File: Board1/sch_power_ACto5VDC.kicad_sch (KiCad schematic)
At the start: 9 parts, among them J1 240VAC

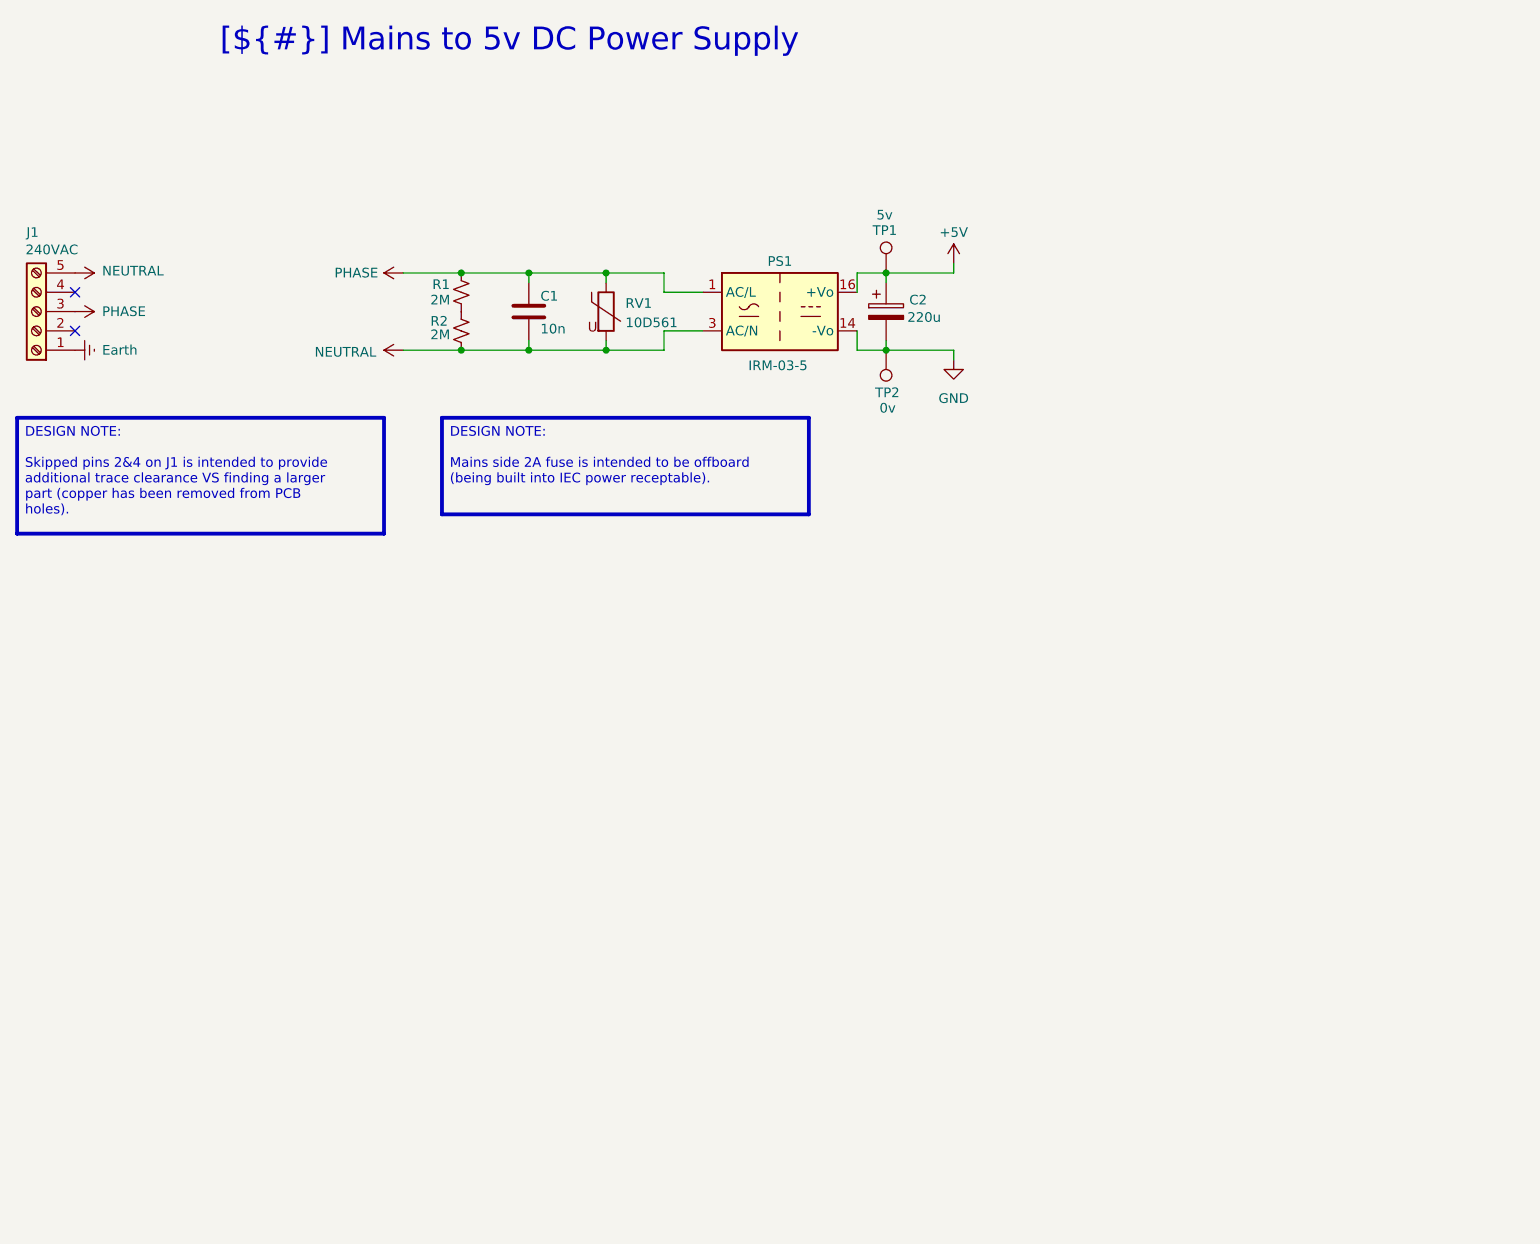
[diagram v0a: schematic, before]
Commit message: Resolve library and ERC issues
No changes to design.
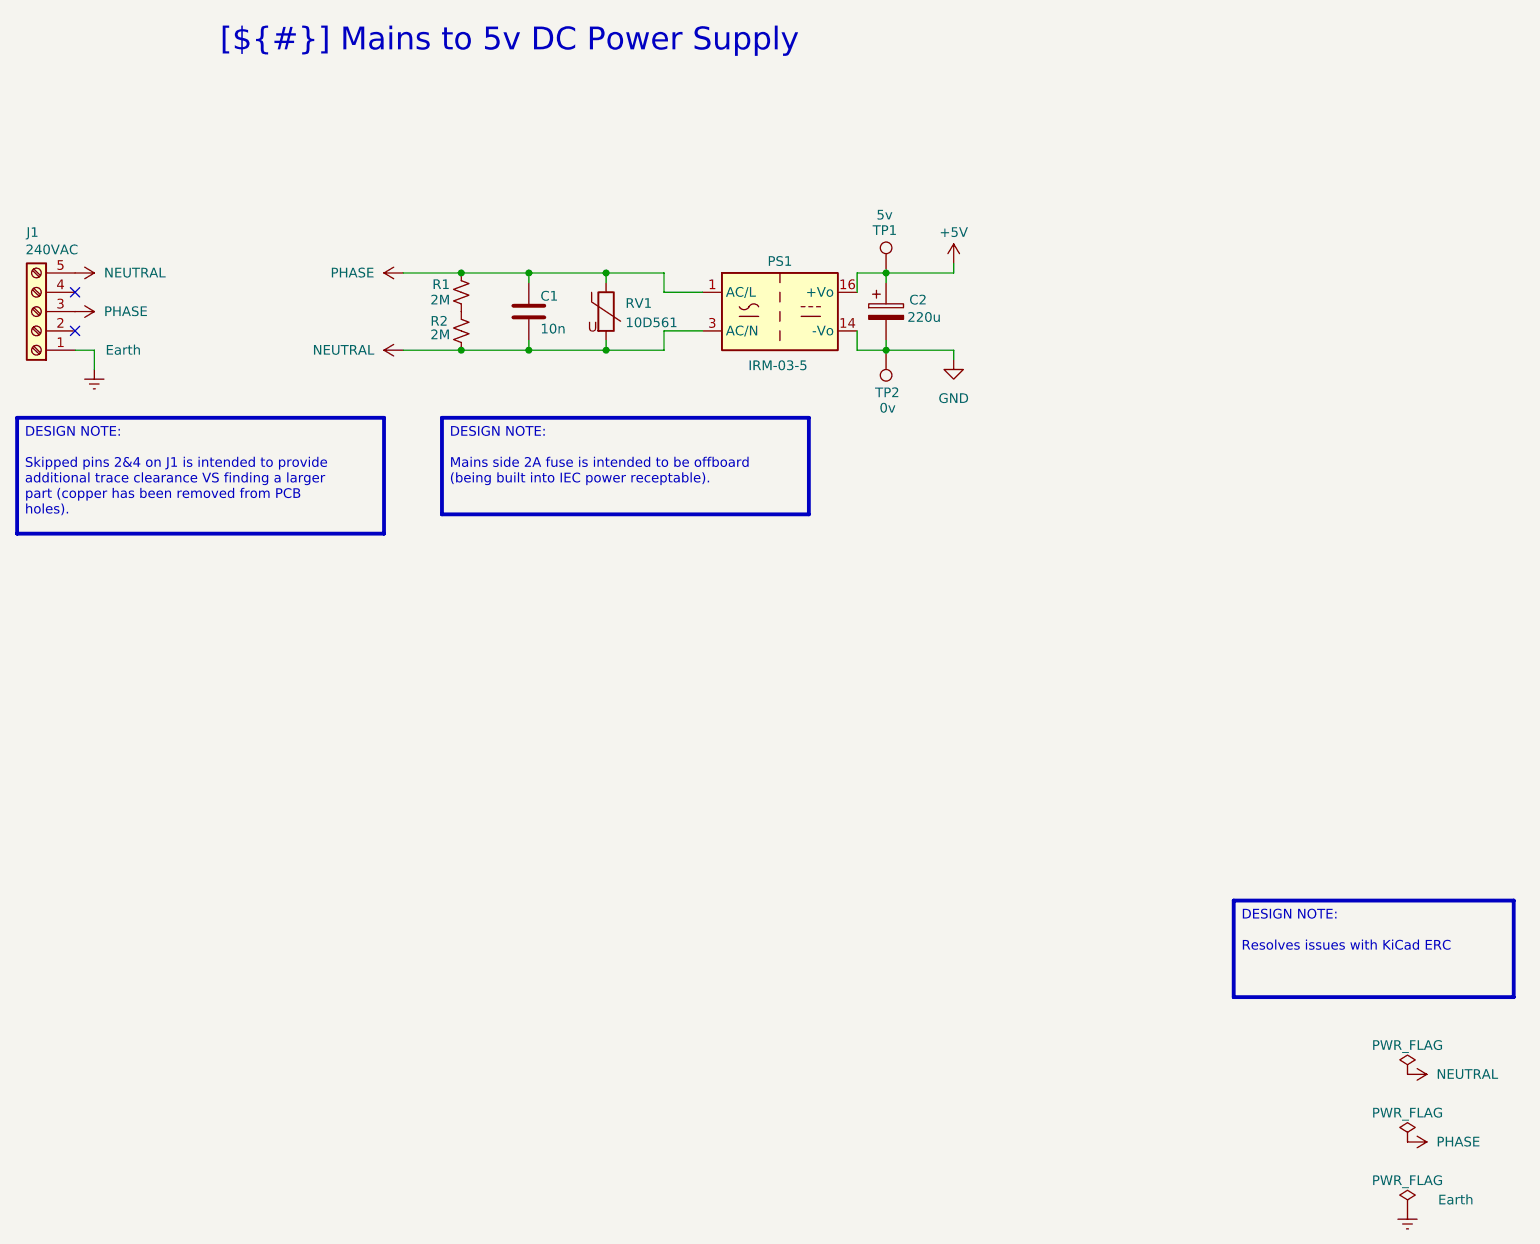
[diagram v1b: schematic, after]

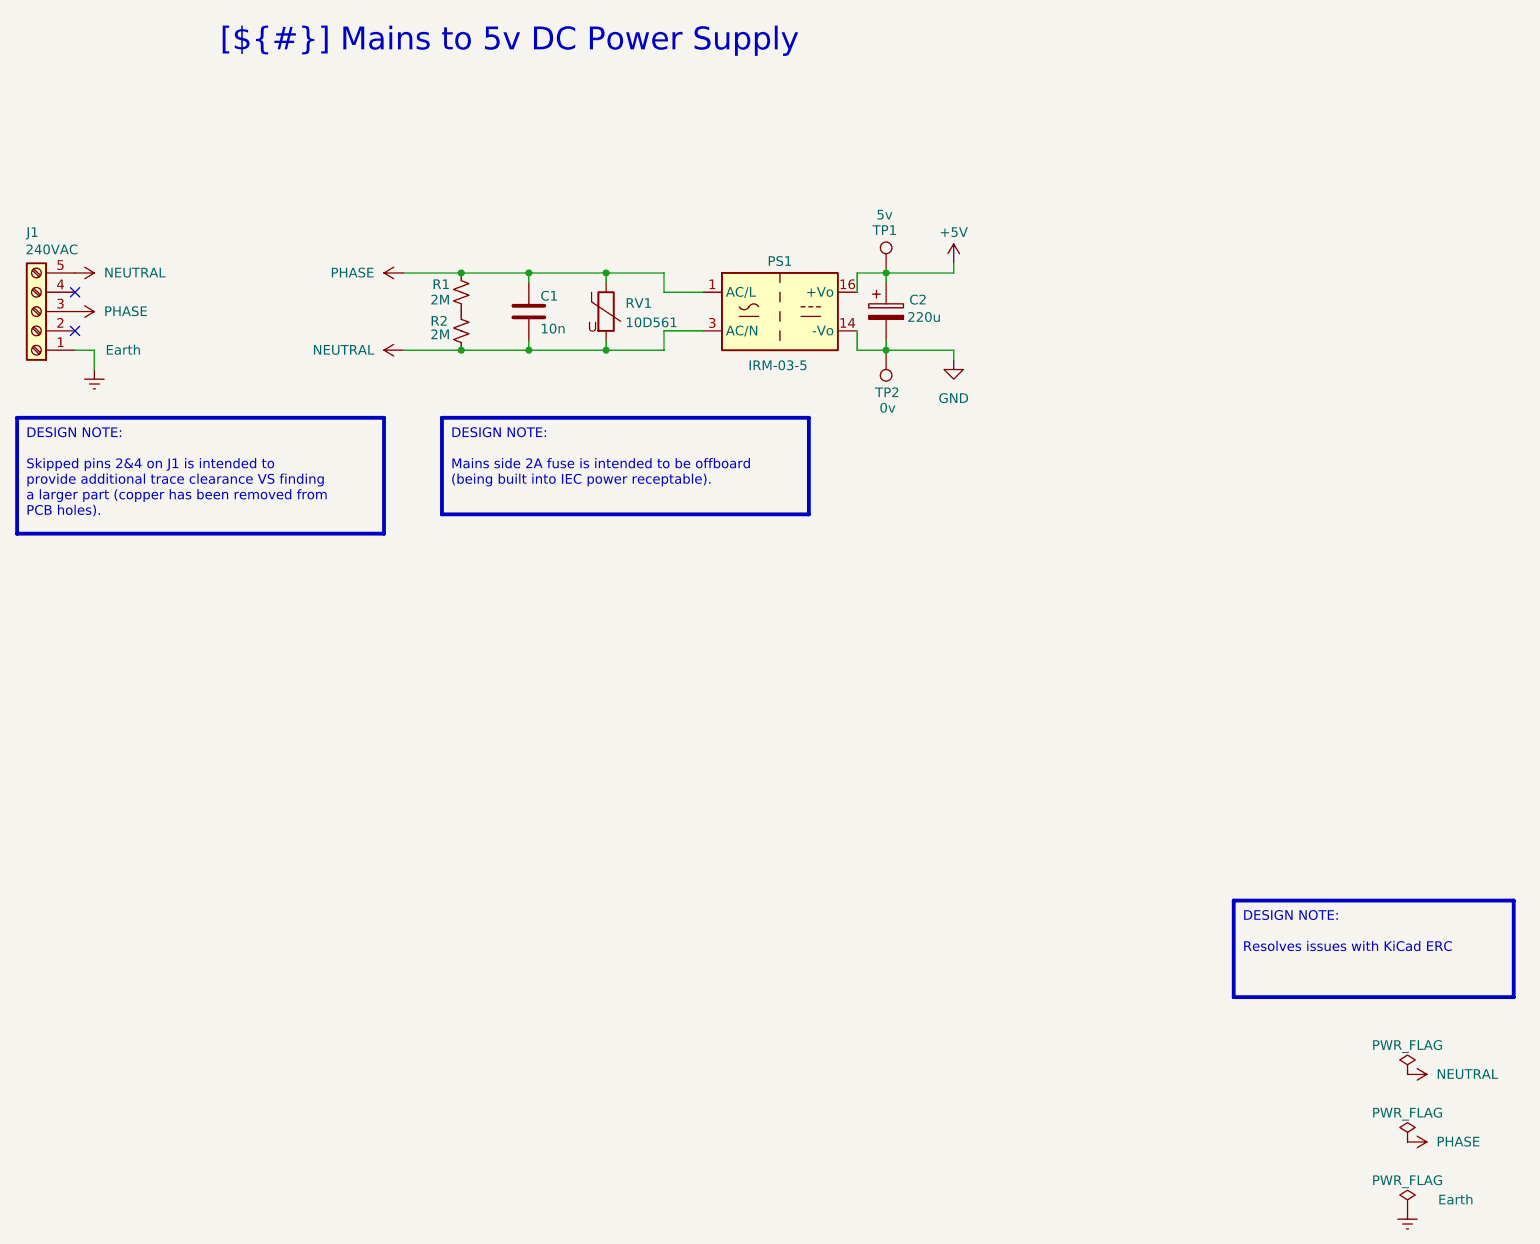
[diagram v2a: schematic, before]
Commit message: Tweaks to schematic for clarity and minor firmware
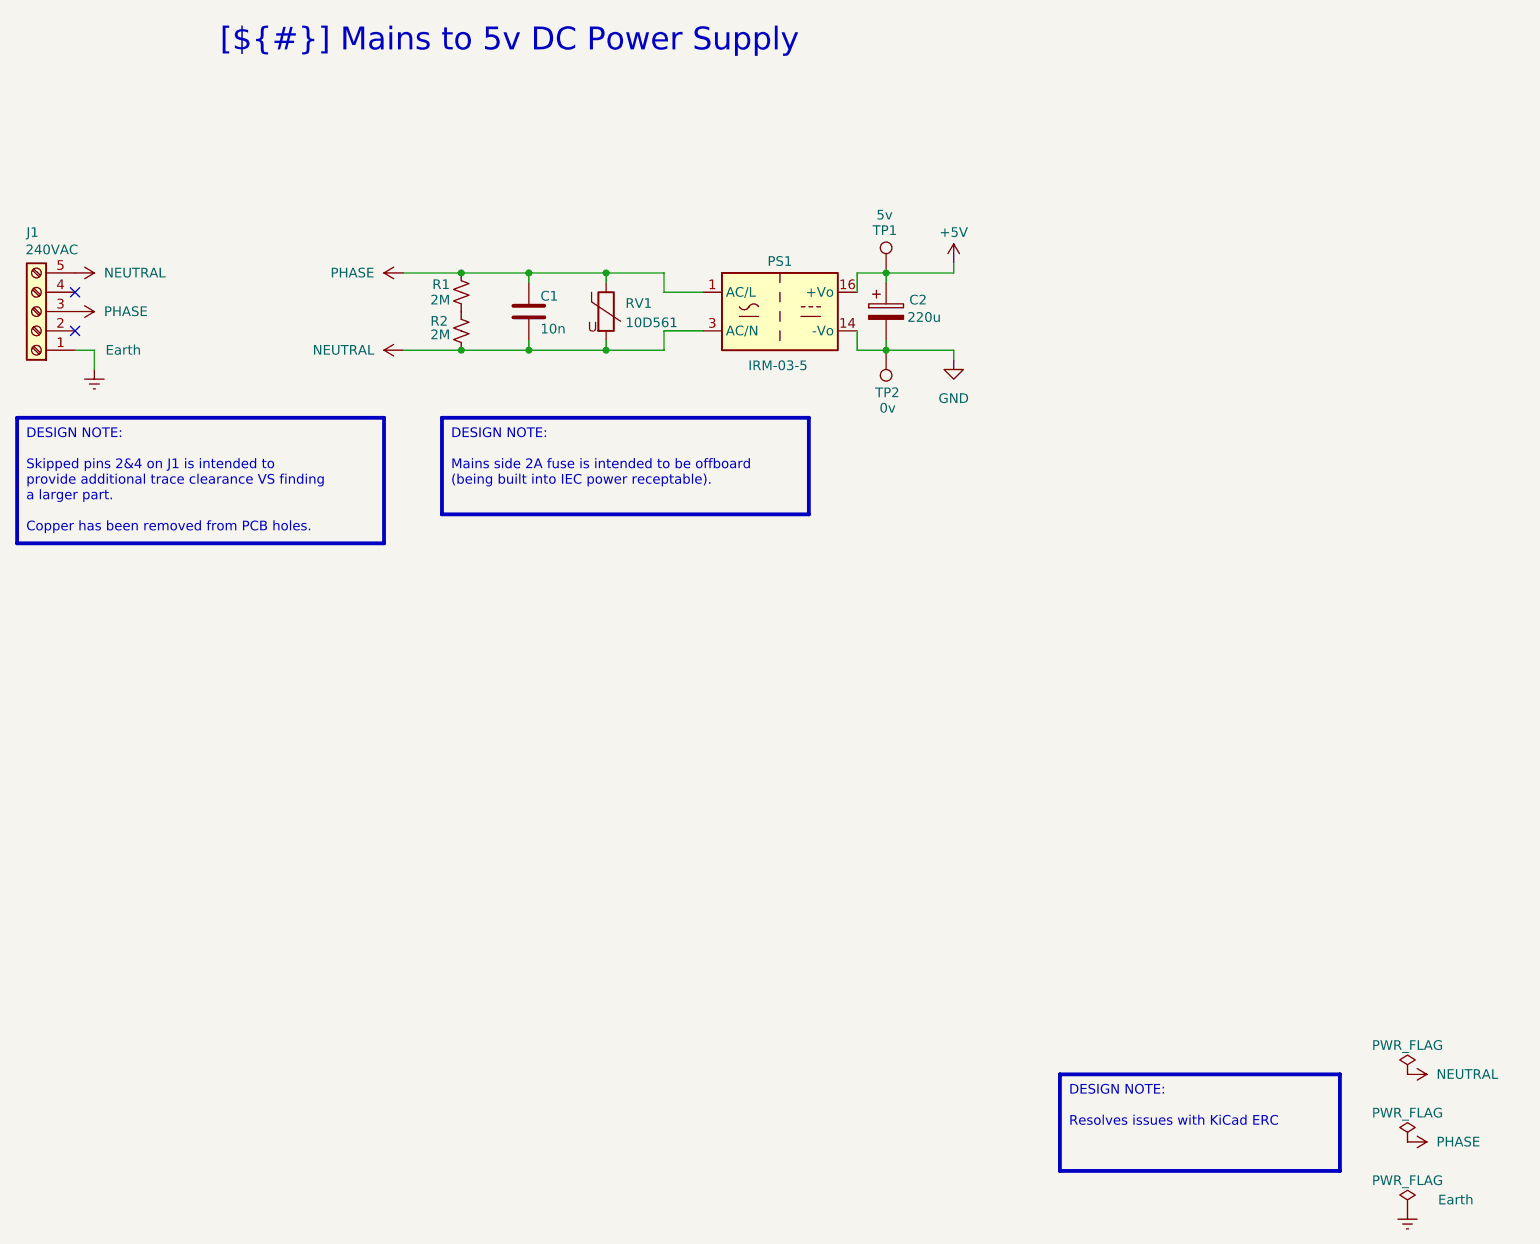
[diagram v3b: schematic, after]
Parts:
- C1: Digikey_PN (none) -> BFC233841103-ND
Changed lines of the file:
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@@
 	(title_block
 		(title "Mains to 5v DC Power Supply")
-		(date "2025-03-08")
+		(date "2025-03-10")
 		(rev "1.2")
 		(company "Wattle Labs")
 	)
-	(text_box "DESIGN NOTE:\n\nSkipped pins 2&4 on J1 is intended to provide additional trace clearance VS finding a larger part (copper has been removed from PCB holes)."
+	(text_box "DESIGN NOTE:\n\nSkipped pins 2&4 on J1 is intended to provide additional trace clearance VS finding a larger part.\n\nCopper has been removed from PCB holes."
 		(exclude_from_sim no)
 		(at 83.82 68.58 0)
-		(size 48.26 15.24)
+		(size 48.26 16.51)
 		(margins 1.2025 1.2025 1.2025 1.2025)
 		(stroke
@@
 	(text_box "DESIGN NOTE:\n\nResolves issues with KiCad ERC"
 		(exclude_from_sim no)
-		(at 243.84 132.08 0)
+		(at 220.98 154.94 0)
 		(size 36.83 12.7)
 		(margins 1.2025 1.2025 1.2025 1.2025)
@@
 			)
 		)
-		(property "Description" "EMI noise supression"
+		(property "Description" "10000 pF Film Capacitor 300V 800V Polypropylene (PP), Metallized Radial"
 			(at 151.13 54.61 0)
 			(effects
@@
 			)
 		)
-		(property "Digikey_PN" ""
+		(property "Digikey_PN" "BFC233841103-ND"
 			(at 151.13 54.61 0)
 			(effects
